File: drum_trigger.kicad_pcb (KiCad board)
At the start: 2 copper layers, 53 parts, among them J6 AudioJack2, J7 AudioJack2, U11 1SS362FV_L3F, U12 1SS362FV_L3F, U13 LM324, U14 1SS362FV_L3F, U15 1SS362FV_L3F, U16 1SS362FV_L3F, U17 1SS362FV_L3F, U18 LM324

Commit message: Initial layout
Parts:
- removed C21, C24, C25, C29, C30, C33: 22pF, Capacitor_SMD:C_0402_1005Metric
- removed C22, C26, C28, C31: 0.22uF, Capacitor_SMD:C_0603_1608Metric
- removed C23, C36: 1000pF, Capacitor_SMD:C_0603_1608Metric
- removed C27, C32: 100pF, Capacitor_SMD:C_0603_1608Metric
- removed C34, C35: 1uF, Capacitor_SMD:C_0603_1608Metric
- removed J6, J7: AudioJack2, Connector_Audio:Jack_6.35mm_Neutrik_NMJ4HCD2_Horizontal
- removed R32, R38, R47, R55: 68k, Resistor_SMD:R_0402_1005Metric
- removed R33, R39, R40, R43, R46, R49, R52, R54: 22k, Resistor_SMD:R_0402_1005Metric
- removed R34, R36, R45, R56: 10k, Resistor_SMD:R_0402_1005Metric
- removed R35, R57: 100, Resistor_SMD:R_0402_1005Metric
- removed R37, R42, R48, R53: 1k, Resistor_SMD:R_0402_1005Metric
- removed R41, R44, R50, R51: 100k, Resistor_SMD:R_0603_1608Metric
- removed R59: 22, Resistor_SMD:R_0402_1005Metric
- removed U11, U12, U14, U15, U16, U17: 1SS362FV_L3F, mod:DIODE_1SS362FV
- removed U13, U18: LM324, Package_SO:SOIC-14_3.9x8.7mm_P1.27mm
- added C1: 0.22uF, Capacitor_SMD:C_0603_1608Metric, F.Cu at (85.9, 74.0)
- added C10: 0.22uF, Capacitor_SMD:C_0603_1608Metric, F.Cu at (204.2, 142.5)
- added C11: 100pF, Capacitor_SMD:C_0603_1608Metric, F.Cu at (208.2, 132.5)
- added C12: 22pF, Capacitor_SMD:C_0402_1005Metric, F.Cu at (203.6, 154.6)
- added C13: 1uF, Capacitor_SMD:C_0603_1608Metric, F.Cu at (79.0, 67.8)
- added C14: 1uF, Capacitor_SMD:C_0603_1608Metric, F.Cu at (90.0, 67.8)
- added C2: 22pF, Capacitor_SMD:C_0402_1005Metric, F.Cu at (78.1, 62.9)
- added C20: 1000pF, Capacitor_SMD:C_0603_1608Metric, F.Cu at (83.1, 74.0)
- added C3: 22pF, Capacitor_SMD:C_0402_1005Metric, F.Cu at (79.1, 71.8)
- added C4: 0.22uF, Capacitor_SMD:C_0603_1608Metric, F.Cu at (64.7, 64.2)
- added C5: 100pF, Capacitor_SMD:C_0603_1608Metric, F.Cu at (61.0, 65.0)
- added C6: 22pF, Capacitor_SMD:C_0402_1005Metric, F.Cu at (73.3, 63.9)
- added C7: 0.22uF, Capacitor_SMD:C_0603_1608Metric, F.Cu at (204.2, 140.0)
- added C8: 22pF, Capacitor_SMD:C_0402_1005Metric, F.Cu at (203.6, 150.7)
- added C9: 22pF, Capacitor_SMD:C_0402_1005Metric, F.Cu at (203.6, 152.7)
- added J4: AudioJack2, Connector_Audio:Jack_6.35mm_Neutrik_NMJ4HFD2_Horizontal, F.Cu at (61.0, 61.0)
- added J5: AudioJack2, Connector_Audio:Jack_6.35mm_Neutrik_NMJ4HFD2_Horizontal, F.Cu at (161.8, 132.9)
- added J8: Conn_01x02_Pin, Connector_JST:JST_PH_B2B-PH-K_1x02_P2.00mm_Vertical, F.Cu at (89.0, 38.0)
- added J9: Conn_01x02_Pin, Connector_JST:JST_PH_B2B-PH-K_1x02_P2.00mm_Vertical, F.Cu at (167.0, 115.5)
- added R1: 10k, Resistor_SMD:R_0402_1005Metric, F.Cu at (73.9, 62.2)
- added R10: 22k, Resistor_SMD:R_0402_1005Metric, F.Cu at (79.2, 70.2)
- added R11: 68k, Resistor_SMD:R_0402_1005Metric, F.Cu at (72.1, 63.9)
- added R12: 10k, Resistor_SMD:R_0402_1005Metric, F.Cu at (70.8, 71.7)
- added R13: 10k, Resistor_SMD:R_0402_1005Metric, F.Cu at (209.8, 119.6)
- added R14: 22k, Resistor_SMD:R_0402_1005Metric, F.Cu at (209.8, 121.5)
- added R15: 68k, Resistor_SMD:R_0402_1005Metric, F.Cu at (209.8, 123.5)
- added R16: 150, Resistor_SMD:R_0402_1005Metric, F.Cu at (84.5, 73.7)
- added R17: 1k, Resistor_SMD:R_0402_1005Metric, F.Cu at (212.7, 113.6)
- added R18: 22k, Resistor_SMD:R_0402_1005Metric, F.Cu at (212.7, 115.6)
- added R19: 100k, Resistor_SMD:R_0603_1608Metric, F.Cu at (212.2, 135.0)
- added R2: 22k, Resistor_SMD:R_0402_1005Metric, F.Cu at (77.9, 74.7)
- added R20: 100k, Resistor_SMD:R_0603_1608Metric, F.Cu at (212.2, 137.5)
- added R21: 22k, Resistor_SMD:R_0402_1005Metric, F.Cu at (212.7, 117.6)
- added R22: 1k, Resistor_SMD:R_0402_1005Metric, F.Cu at (212.7, 119.6)
- added R23: 22k, Resistor_SMD:R_0402_1005Metric, F.Cu at (212.7, 121.5)
- added R24: 68k, Resistor_SMD:R_0402_1005Metric, F.Cu at (212.7, 123.5)
- added R25: 10k, Resistor_SMD:R_0402_1005Metric, F.Cu at (212.7, 125.5)
- added R3: 68k, Resistor_SMD:R_0402_1005Metric, F.Cu at (76.9, 62.9)
- added R4: 1k, Resistor_SMD:R_0402_1005Metric, F.Cu at (71.1, 68.5)
- added R5: 22k, Resistor_SMD:R_0402_1005Metric, F.Cu at (74.5, 66.5)
- added R6: 100k, Resistor_SMD:R_0603_1608Metric, F.Cu at (68.5, 66.2)
- added R7: 100k, Resistor_SMD:R_0603_1608Metric, F.Cu at (65.5, 67.0)
- added R8: 22k, Resistor_SMD:R_0402_1005Metric, F.Cu at (79.2, 69.1)
- added R9: 1k, Resistor_SMD:R_0402_1005Metric, F.Cu at (76.5, 67.9)
- added U1: 1SS362FV_L3F, mod:DIODE_1SS362FV, F.Cu at (75.2, 64.0)
- added U2: 1SS362FV_L3F, mod:DIODE_1SS362FV, F.Cu at (75.9, 72.6)
- added U3: LM2902PWR, Package_SO:SOIC-14_3.9x8.7mm_P1.27mm, F.Cu at (84.5, 67.8)
- added U4: 1SS362FV_L3F, mod:DIODE_1SS362FV, F.Cu at (78.7, 65.3)
- added U5: 1SS362FV_L3F, mod:DIODE_1SS362FV, F.Cu at (203.8, 123.5)
- added U6: 1SS362FV_L3F, mod:DIODE_1SS362FV, F.Cu at (203.8, 126.6)
- added U7: 1SS362FV_L3F, mod:DIODE_1SS362FV, F.Cu at (203.8, 129.7)
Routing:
- net Net-(U3A--): track 0.00 -> 6.00 mm
- net Net-(C2-Pad2): track 0.00 -> 3.90 mm
- net Net-(U3B-+): track 0.00 -> 3.46 mm
- net Net-(U3B--): track 0.00 -> 3.35 mm
- net Net-(C3-Pad2): track 0.00 -> 3.32 mm

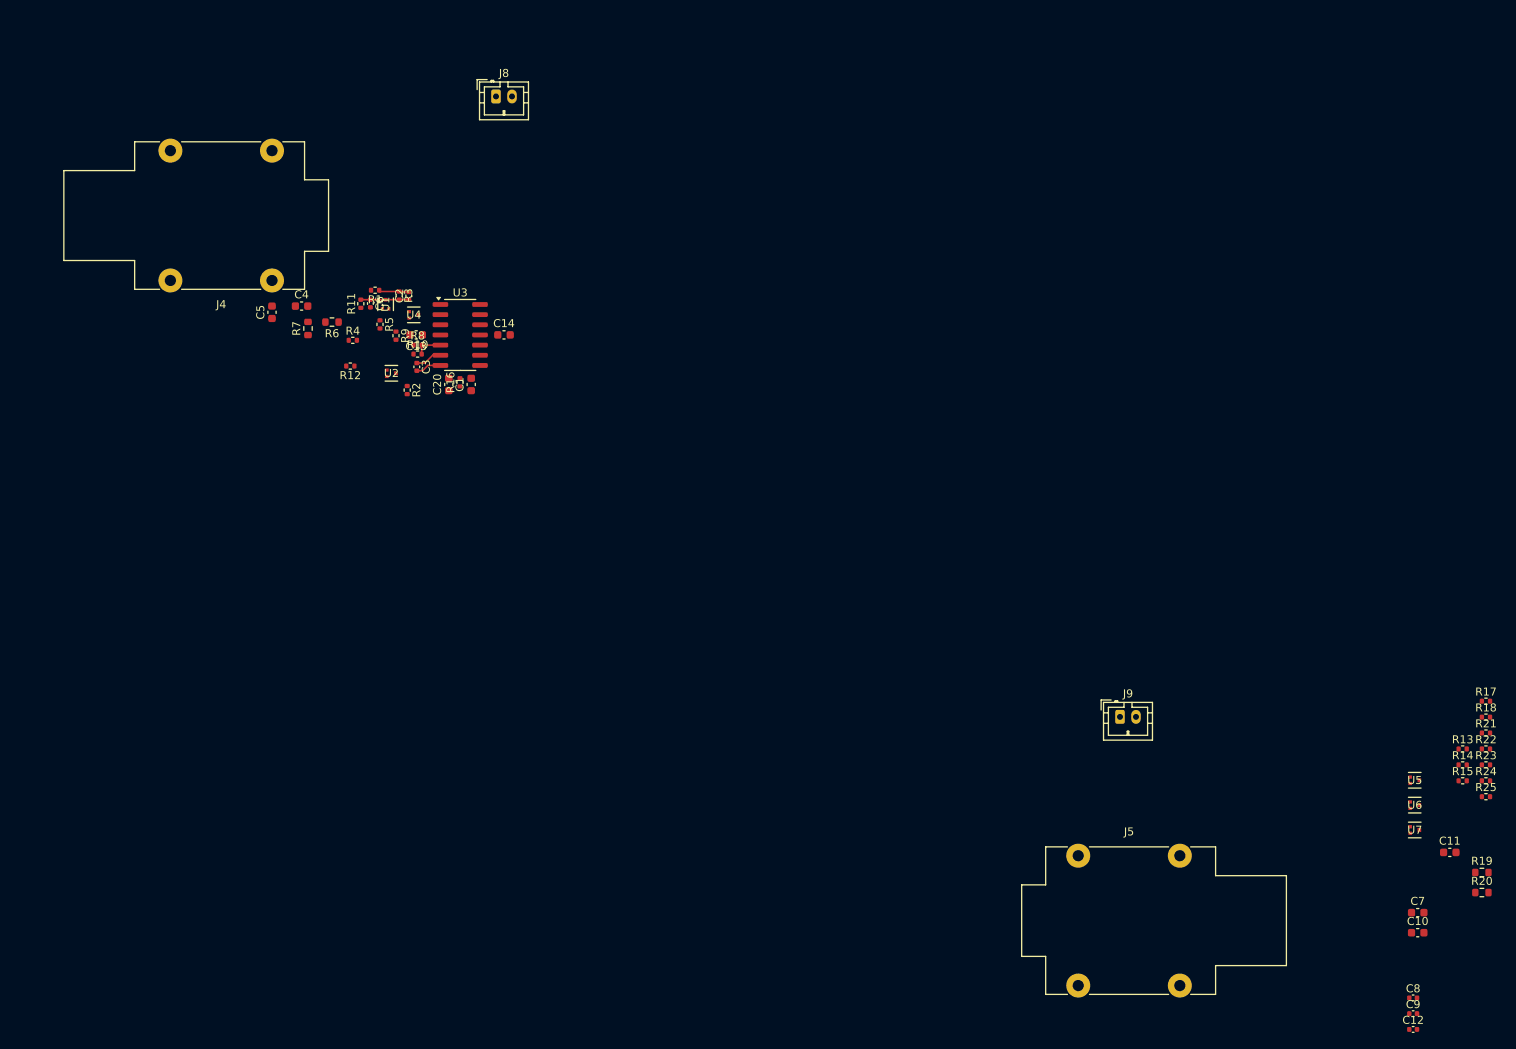
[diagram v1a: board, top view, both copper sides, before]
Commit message: Double trigger layout to test
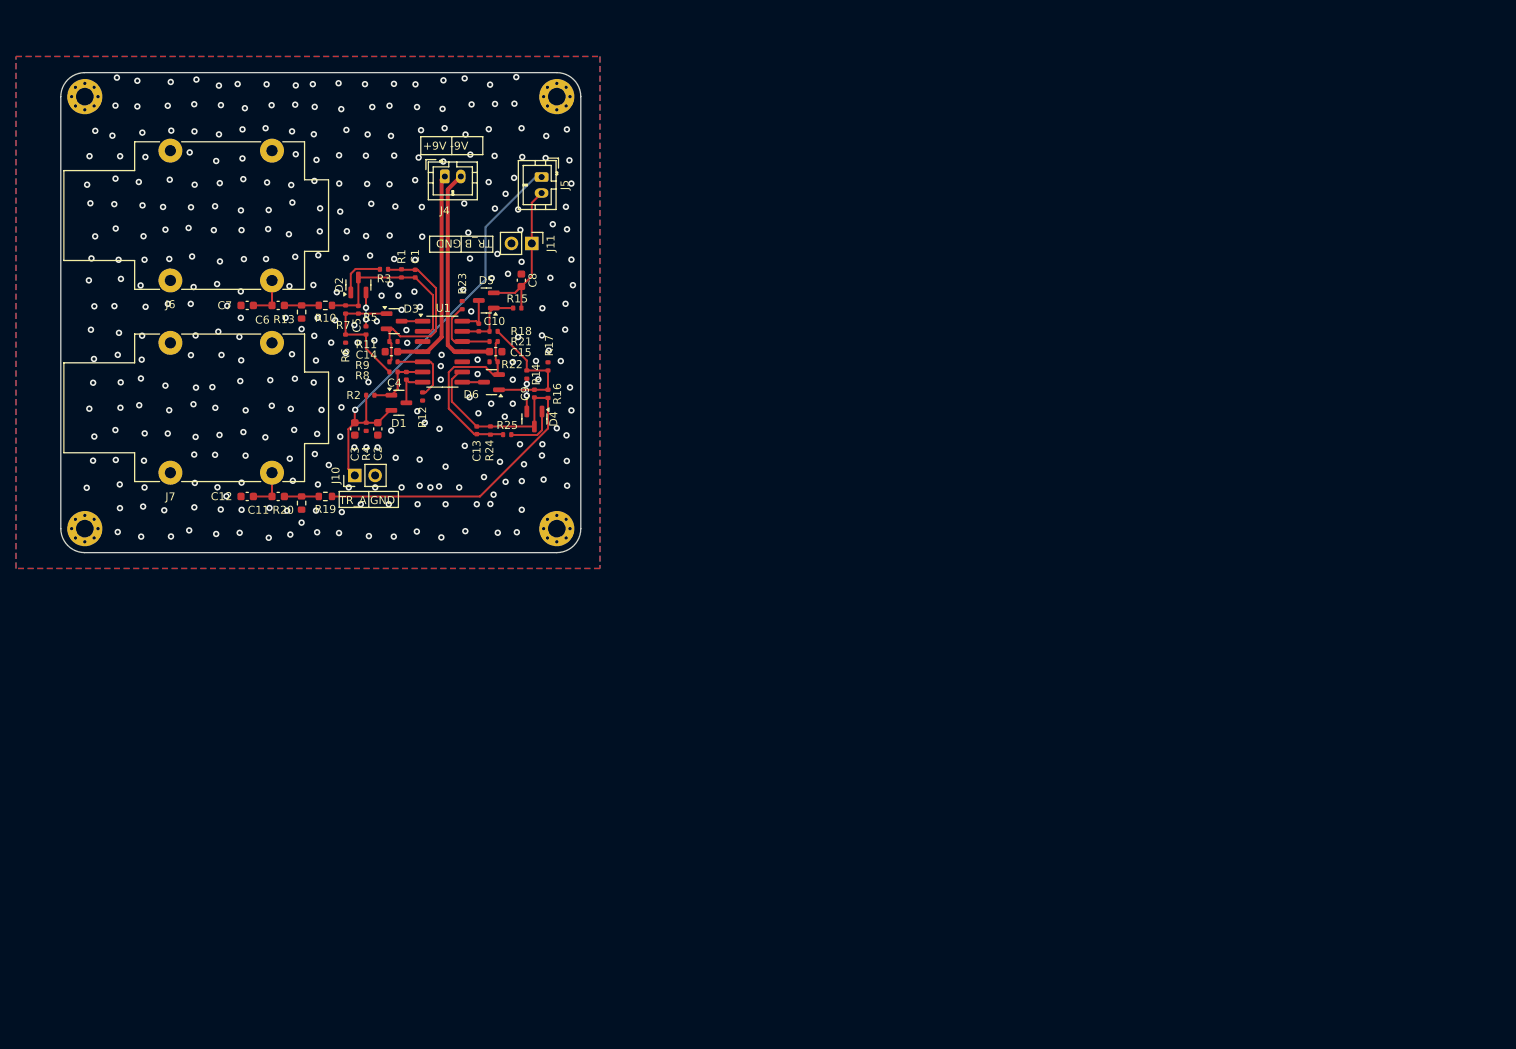
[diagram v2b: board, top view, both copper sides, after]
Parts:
- removed J9: Conn_01x02_Pin, Connector_JST:JST_PH_B2B-PH-K_1x02_P2.00mm_Vertical
- removed the U1 at (75.2, 64.0)
- removed U2, U4, U5, U6, U7: 1SS362FV_L3F, mod:DIODE_1SS362FV
- added D1: BAV99, Package_TO_SOT_SMD:SOT-23, F.Cu at (76.9, 76.3)
- added D2: BAV99, Package_TO_SOT_SMD:SOT-23, F.Cu at (71.8, 61.6)
- added D3: BAV99, Package_TO_SOT_SMD:SOT-23, F.Cu at (76.3, 66.1)
- added D4: BAV99, Package_TO_SOT_SMD:SOT-23, F.Cu at (93.8, 78.3)
- added D5: BAV99, Package_TO_SOT_SMD:SOT-23, F.Cu at (87.8, 63.5)
- added D6: BAV99, Package_TO_SOT_SMD:SOT-23, F.Cu at (88.4, 73.7)
- added H1: MountingHole_Pad, MountingHole:MountingHole_2.2mm_M2_Pad_Via, F.Cu at (37.6, 38.0)
- added H2: MountingHole_Pad, MountingHole:MountingHole_2.2mm_M2_Pad_Via, F.Cu at (96.6, 38.0)
- added H3: MountingHole_Pad, MountingHole:MountingHole_2.2mm_M2_Pad_Via, F.Cu at (96.6, 92.0)
- added H4: MountingHole_Pad, MountingHole:MountingHole_2.2mm_M2_Pad_Via, F.Cu at (37.6, 92.0)
- added J10: Conn_01x02_Pin, Connector_PinHeader_2.54mm:PinHeader_1x02_P2.54mm_Vertical, F.Cu at (71.3, 85.4)
- added J11: Conn_01x02_Pin, Connector_PinHeader_2.54mm:PinHeader_1x02_P2.54mm_Vertical, F.Cu at (93.5, 56.4)
- added J5: Conn_01x02_Pin, Connector_JST:JST_PH_B2B-PH-K_1x02_P2.00mm_Vertical, F.Cu at (94.7, 48.1)
- C1: renamed from C2; footprint Capacitor_SMD:C_0402_1005Metric -> C_0402_custom:C_0402_1005Metric
- C10: renamed from C9; footprint Capacitor_SMD:C_0402_1005Metric -> C_0402_custom:C_0402_1005Metric
- C13: renamed from C12; footprint Capacitor_SMD:C_0402_1005Metric -> C_0402_custom:C_0402_1005Metric
- C4: renamed from C3; footprint Capacitor_SMD:C_0402_1005Metric -> C_0402_custom:C_0402_1005Metric
- C5: renamed from C6; footprint Capacitor_SMD:C_0402_1005Metric -> C_0402_custom:C_0402_1005Metric
- C9: renamed from C8; footprint Capacitor_SMD:C_0402_1005Metric -> C_0402_custom:C_0402_1005Metric
- R1: renamed from R3; footprint Resistor_SMD:R_0402_1005Metric -> R_0402_custom:R_0402_1005Metric
- R11: renamed from R9; footprint Resistor_SMD:R_0402_1005Metric -> R_0402_custom:R_0402_1005Metric
- R12: renamed from R10; footprint Resistor_SMD:R_0402_1005Metric -> R_0402_custom:R_0402_1005Metric
- R14: renamed from R13; footprint Resistor_SMD:R_0402_1005Metric -> R_0402_custom:R_0402_1005Metric
- R15: renamed from R14; footprint Resistor_SMD:R_0402_1005Metric -> R_0402_custom:R_0402_1005Metric
- R16: renamed from R15; footprint Resistor_SMD:R_0402_1005Metric -> R_0402_custom:R_0402_1005Metric
- R17, R18, R2, R21, R22, R23, R24, R25: footprint Resistor_SMD:R_0402_1005Metric -> R_0402_custom:R_0402_1005Metric
- R3: renamed from R1; footprint Resistor_SMD:R_0402_1005Metric -> R_0402_custom:R_0402_1005Metric
- R4: renamed from R16; footprint Resistor_SMD:R_0402_1005Metric -> R_0402_custom:R_0402_1005Metric
- R5: renamed from R12; footprint Resistor_SMD:R_0402_1005Metric -> R_0402_custom:R_0402_1005Metric
- R6: renamed from R4; footprint Resistor_SMD:R_0402_1005Metric -> R_0402_custom:R_0402_1005Metric
- R7: renamed from R11; footprint Resistor_SMD:R_0402_1005Metric -> R_0402_custom:R_0402_1005Metric
- R8: renamed from R5; footprint Resistor_SMD:R_0402_1005Metric -> R_0402_custom:R_0402_1005Metric
- R9: renamed from R8; footprint Resistor_SMD:R_0402_1005Metric -> R_0402_custom:R_0402_1005Metric
- moved C12 156.8 mm to (57.9, 88.0)
- moved R20 155.4 mm to (64.7, 88.8), turned to 90 degrees
- moved C11 152.5 mm to (61.8, 88.0)
- moved R19 152.0 mm to (67.7, 88.0), turned to 180 degrees
- moved C10 144.9 mm to (86.8, 66.9), turned to 90 degrees
- moved R23 140.3 mm to (84.8, 64.1), turned to -90 degrees
- moved C13 139.0 mm to (86.6, 79.7), turned to -90 degrees
- moved C8 137.1 mm to (92.2, 61.0), turned to -90 degrees
- moved R21 133.4 mm to (88.7, 68.6), turned to 180 degrees
- moved C9 133.3 mm to (93.8, 75.1), turned to 90 degrees
- moved R22 133.1 mm to (88.7, 71.2), turned to 180 degrees
- moved R18 133.1 mm to (88.7, 67.4), turned to 180 degrees
- moved R24 131.9 mm to (88.3, 79.8), turned to 90 degrees
- moved R15 131.2 mm to (91.7, 64.5)
- moved R25 130.4 mm to (90.4, 80.3)
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- renumbered C10 to C11, C11 to C12, C13 to C14, C14 to C15, C1 to C2, C20 to C3, C4 to C6, C5 to C7, C7 to C8, J8 to J4, J4 to J6, J5 to J7, R6 to R10, R7 to R13, U3 to U1
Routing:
- net /TriggerPair/TRIG_A_OUT: track 0.00 -> 57.3 mm, vias 0 -> 1
- net Net-(U1C--): track 0.00 -> 55.8 mm
- net -9V: track 0.00 -> 27.3 mm
- net +9V: track 0.00 -> 26.5 mm
- net Net-(D6-A): track 0.00 -> 24.0 mm
- net Net-(D3-A): track 3.90 -> 23.7 mm
- net /TriggerPair/TRIG_B_OUT: track 0.00 -> 19.2 mm
- net Net-(C9-Pad2): track 0.00 -> 17.6 mm
- net Net-(U1A--): track 6.00 -> 22.8 mm
- net Net-(C5-Pad2): track 0.17 -> 16.2 mm
- net Net-(U1D-+): track 0.00 -> 9.19 mm
- net Net-(U1D--): track 0.00 -> 8.97 mm
- net Net-(D4-K-Pad1): track 0.00 -> 6.45 mm
- net Net-(D2-K-Pad1): track 0.00 -> 6.25 mm
- net /TriggerPair/TRIG_A_IN: track 0.00 -> 5.45 mm
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- added copper zone on B.Cu, net GND
- added copper zone on F.Cu, net GND
- added copper zone on In1.Cu, net GND
- added copper zone on In2.Cu, net GND
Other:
- board outline added: 65 x 60 mm
- copper layers 2 -> 4
- board text added: "+9V -9V"
- board text added: "TR_A GND"
- board text added: "TR_B GND"

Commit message: Production ready pcb
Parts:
- added D7: LED, LED_SMD:LED_0805_2012Metric, F.Cu at (74.0, 48.0)
- added R59: 1.5k, Resistor_SMD:R_0603_1608Metric, F.Cu at (77.4, 48.0)
- added R60: 100, R_0402_custom:R_0402_1005Metric, F.Cu at (73.1, 77.2)
- R1, R16, R24, R7: footprint R_0402_custom:R_0402_1005Metric -> Resistor_SMD:R_0603_1608Metric
- R4: value 150 -> 100
- moved R2 0.60 mm to (72.7, 75.3)
- moved C2 0.60 mm to (73.6, 79.6)
- moved C3 0.60 mm to (70.8, 79.6)
- moved R4 0.60 mm to (72.2, 79.3)
- moved R1 0.45 mm to (77.2, 59.7)
- moved R16 0.38 mm to (95.5, 74.8)
- moved R24 0.31 mm to (88.3, 80.1)
- moved R7 0.31 mm to (70.2, 64.9)
- moved C1 0.14 mm to (78.9, 60.0)
- moved D2 0.13 mm to (71.8, 61.4)
- moved R3 0.13 mm to (75.0, 59.5)
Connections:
- C2 pad 2: /TriggerPair/TRIG_A_OUT -> Net-(D1-A)
- D1 pad 2: /TriggerPair/TRIG_A_OUT -> Net-(D1-A)
- R2 pad 2: /TriggerPair/TRIG_A_OUT -> Net-(D1-A)
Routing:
- net Net-(D1-A): track 0.00 -> 6.34 mm
- net /TriggerPair/TRIG_A_OUT: track 57.3 -> 51.8 mm
- net +9V: track 26.5 -> 31.2 mm
- net Net-(D7-A): track 0.00 -> 1.89 mm
- net Net-(D6-A): track 24.0 -> 24.6 mm
- net Net-(D3-A): track 23.7 -> 24.3 mm
- net Net-(U1B--): track 8.48 -> 9.08 mm
- net GND: vias 342 -> 340

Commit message: Minor upates to the pcb
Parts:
- added FB3: FerriteBead_Small, Inductor_SMD:L_0805_2012Metric, F.Cu at (94.8, 59.1)
- added FB4: FerriteBead_Small, Inductor_SMD:L_0805_2012Metric, F.Cu at (94.8, 82.9)
- C11, C2, C6, C8: value 0.22uF -> 220nF
- C3: value 1000pF -> 1nF
- D1, D2, D3, D4, D5, D6: value BAV99 -> BAV99,215
- D7: value LED -> KT-0805G
- moved C7 37.3 mm to (95.1, 60.9)
- moved C12 37.3 mm to (95.1, 84.9)
- moved R14 37.2 mm to (129.7, 67.7)
- moved C13 37.2 mm to (123.5, 74.7)
- moved C14 37.2 mm to (112.8, 64.8)
- moved C15 37.2 mm to (125.8, 64.8)
- moved C2 37.2 mm to (110.5, 74.5)
- moved C3 37.2 mm to (107.6, 74.5)
- moved C8 37.2 mm to (129.0, 55.9)
- moved D2 37.2 mm to (108.7, 56.4)
- moved D3 37.2 mm to (113.1, 61.0)
- moved D5 37.2 mm to (124.6, 58.4)
- moved D7 37.2 mm to (110.9, 42.9)
- moved H2 37.2 mm to (133.5, 33.0)
- moved H3 37.2 mm to (133.5, 87.0)
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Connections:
- C11 pad 1: /TriggerPair/TRIG_B_IN -> Net-(C11-Pad1)
- C12 pad 2: /TriggerPair/TRIG_B_IN -> Net-(C11-Pad1)
- C6 pad 1: /TriggerPair/TRIG_A_IN -> Net-(C6-Pad1)
- C7 pad 2: /TriggerPair/TRIG_A_IN -> Net-(C6-Pad1)
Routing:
- net Net-(C11-Pad1): track 0.00 -> 3.97 mm
- net Net-(C6-Pad1): track 0.00 -> 3.85 mm
- net GND: vias 340 -> 326

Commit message: Simulation fixes + board fixes
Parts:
- removed J5: Conn_01x02_Pin, Connector_JST:JST_PH_B2B-PH-K_1x02_P2.00mm_Vertical
- removed R4, R60: 100, R_0402_custom:R_0402_1005Metric
- added J12: Conn_01x03_Pin, Connector_JST:JST_PH_B3B-PH-K_1x03_P2.00mm_Vertical, F.Cu at (119.5, 43.0)
- FB3, FB4: value FerriteBead_Small -> 600
- J4: value Conn_01x02_Pin -> Conn_01x03_Pin; footprint Connector_JST:JST_PH_B2B-PH-K_1x02_P2.00mm_Vertical -> Connector_JST:JST_PH_B3B-PH-K_1x03_P2.00mm_Vertical
- moved J4 12.9 mm to (132.1, 40.3), turned to -90 degrees
- moved C2 1.60 mm to (110.1, 73.0)
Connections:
- C2 pad 2: Net-(D1-A) -> /TriggerPair/TRIG_A_OUT
- D1 pad 2: Net-(D1-A) -> /TriggerPair/TRIG_A_OUT
- J4 pad 1: +9V -> /TriggerPair/TRIG_A_OUT
- J4 pad 2: -9V -> /TriggerPair/TRIG_B_OUT
- R2 pad 2: Net-(D1-A) -> /TriggerPair/TRIG_A_OUT
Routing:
- net Net-(D1-A): track 6.34 -> 0.00 mm
- net /TriggerPair/TRIG_A_OUT: track 51.8 -> 57.8 mm
- net /TriggerPair/TRIG_B_OUT: track 19.2 -> 22.2 mm
- net -9V: track 27.3 -> 28.1 mm
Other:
- board text added: "+Vin"
- board text added: "-Vin"
- board text added: "A"
- board text added: "B"
- board text added: "G"
- board text removed: "+9V -9V"
